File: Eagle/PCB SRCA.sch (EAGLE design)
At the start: 75 parts, among them IC1 DSPIC30F4011-30I_P, IC2 LM324LVIDR, IC3 LMT86QDCKRQ1, IC4 FT232RL-REEL, J1 TBL002A-350-03GR-2OR, J2 TBL002A-350-03GR-2OR, J3 TBL002A-350-03GR-2OR, J4 44914-0801, J5 TBL002A-350-03GR-2OR, J6 44914-0401, Q1 TIP41C, T1 2N3904, T12 2N3904, T13 2N3904, T2 2N3904, T3 2N3904, T4 2N3904, T5 2N3904, T6 2N3904, T7 2N3904

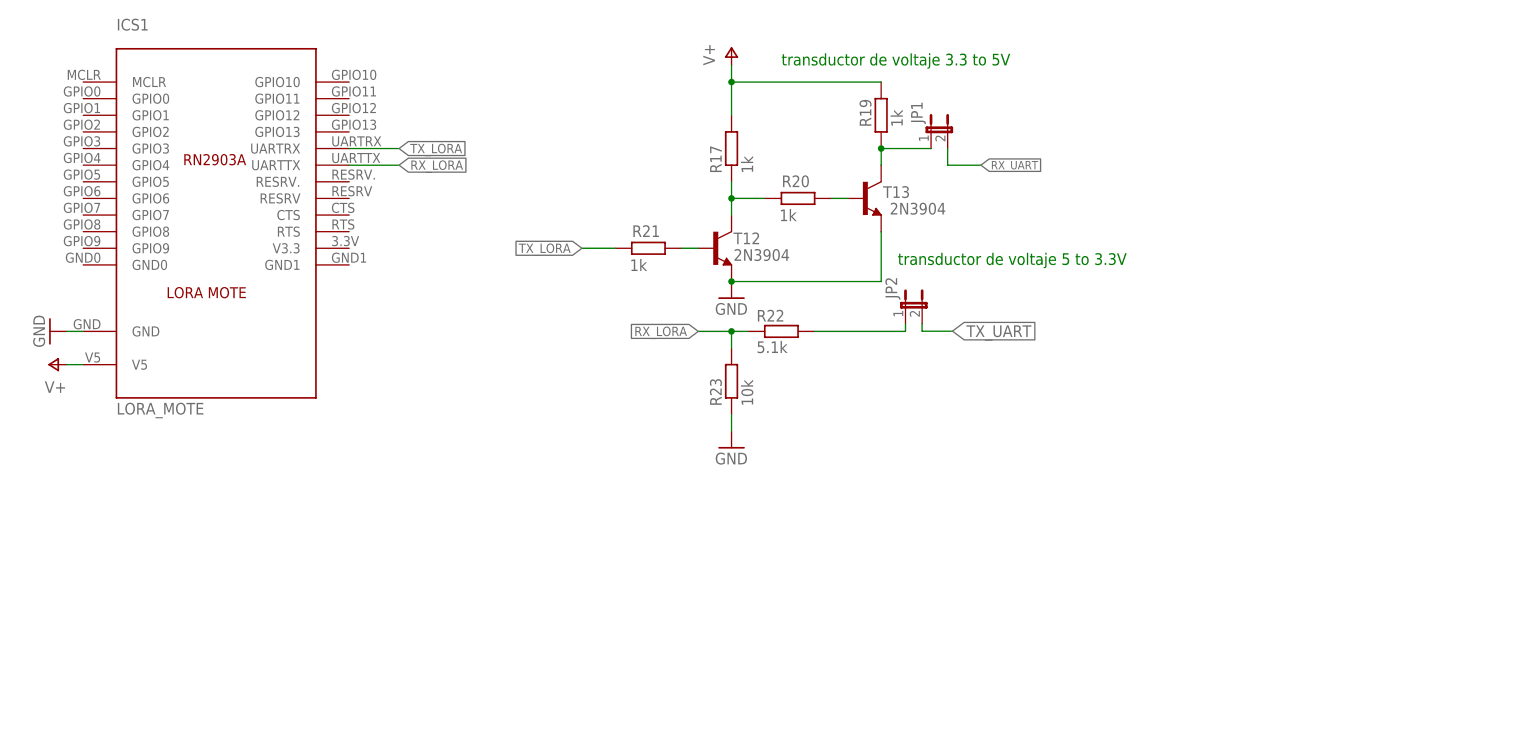
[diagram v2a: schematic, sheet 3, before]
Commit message: 31-08-2021
se agregaron las librerías del proyecto se hizo algunas correciones en la parte de el sensor de temperatura y se hizo se coloco un regulador de 5V a 3.3V para la lora mote
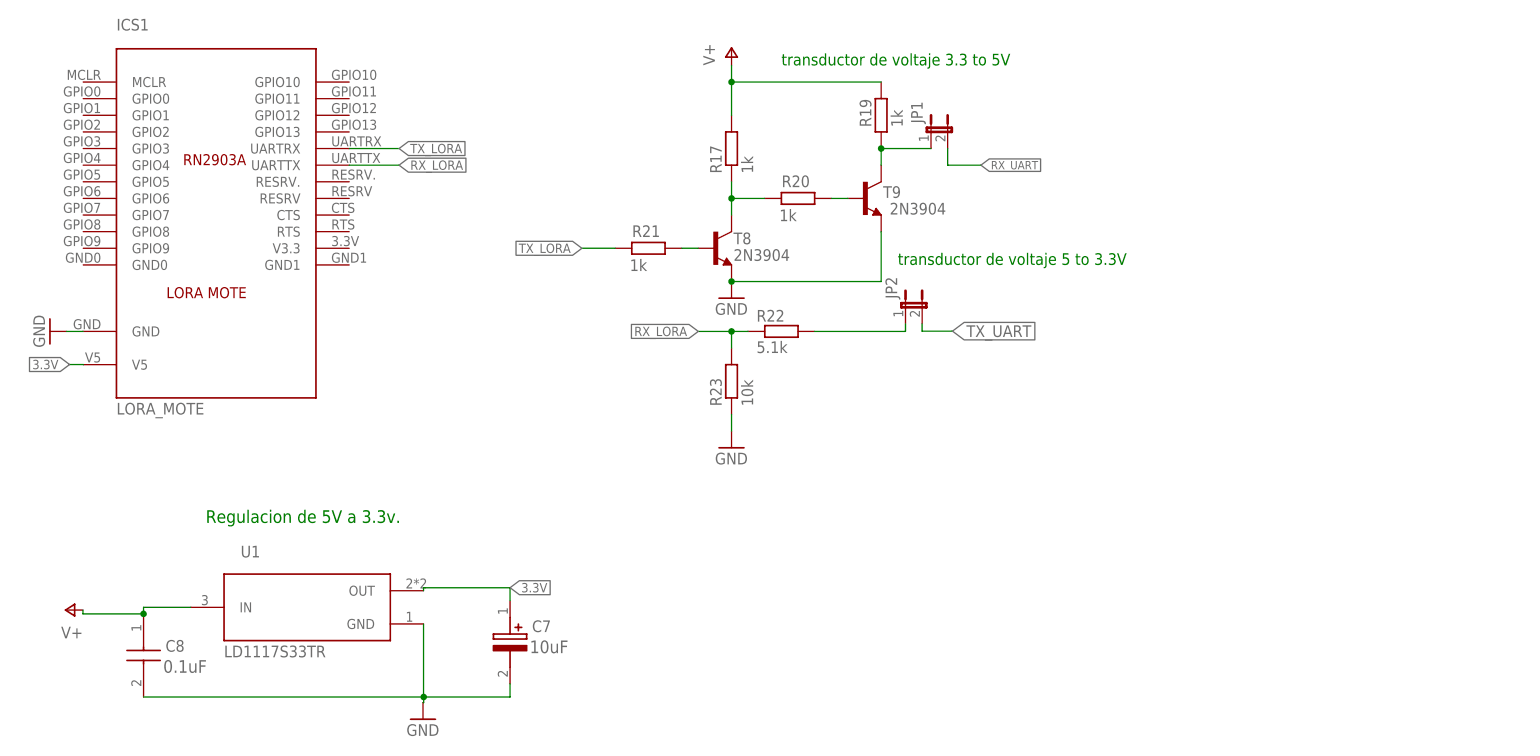
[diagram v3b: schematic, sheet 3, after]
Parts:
- added C7: UUP1C100MCL1GS, UUP1C100MCL1GS:UUP1C100MCL1GS
- added C8: C0805X104K1RAC3316, C0805X104K1RAC3316:C0805X104K1RAC3316
- added R27: RC0805FR-071KL, RC0805FR-071KL:RC0805FR-071KL
- added U1: LD1117S33TR, LD1117S33TR:LD1117S33TR
- renumbered T12 to T8, T13 to T9
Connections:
- new net 3.3V: C7.+, ICS1.V5, U1.OUT
- new net N$14: IC3.OUT, R27.2
- net GND: now also C7.-, C8.2, U1.GND
- net N$27: now also R27.1; no longer IC3.OUT
- net V+: now also C8.1, U1.IN; no longer ICS1.V5
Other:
- note added: "0.1uF"
- note added: "1.5k"
- note added: "Regulacion de 5V a 3.3v."
- moved on the sheet: C1, C5

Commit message: 04-09-2021
cambios de la nueva pcb se agrego cambios del uart entre dspic y lora
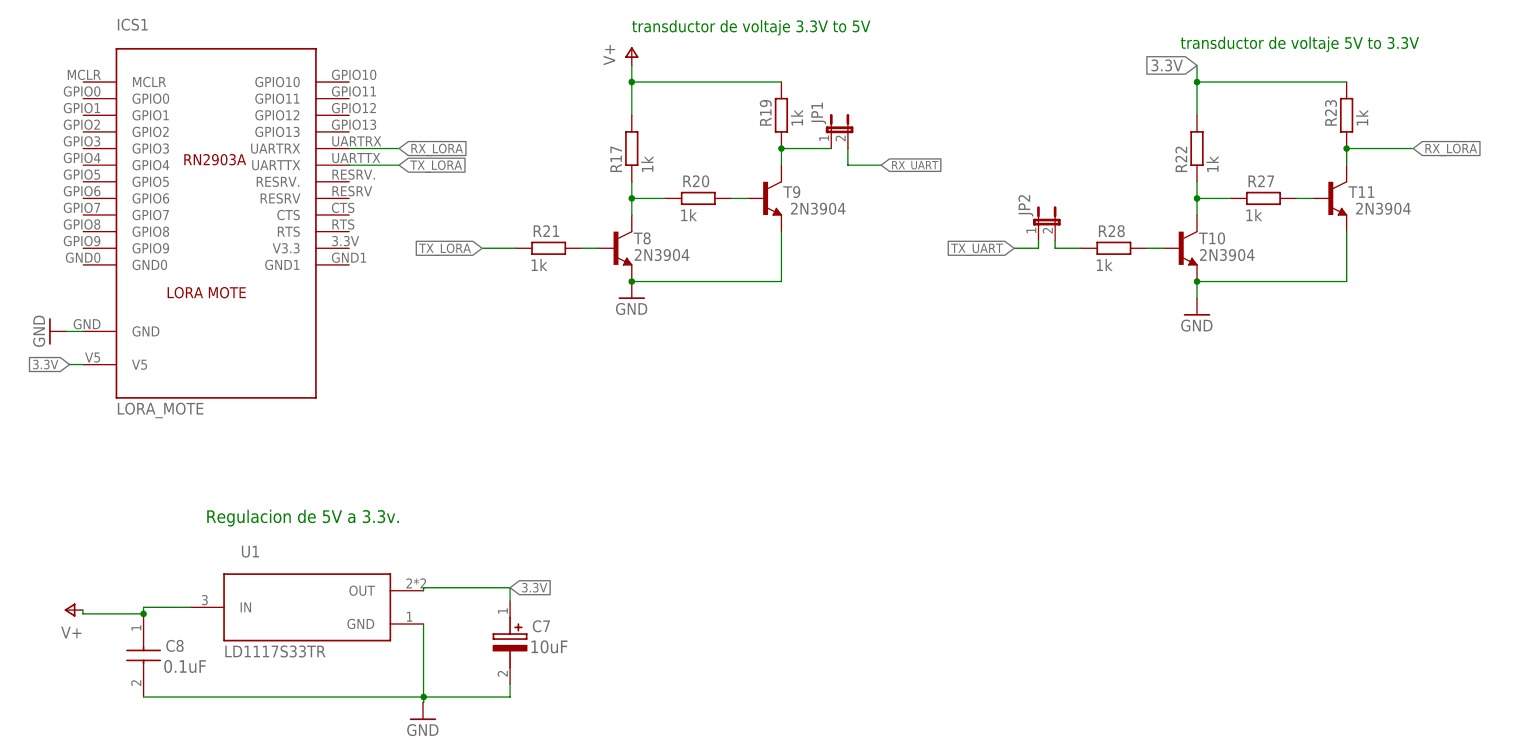
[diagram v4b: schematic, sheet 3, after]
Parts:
- removed C1: (no value), rcl:C-EUC0805
- added R28: 1k, rcl:R-EU_0207/10
- added T10, T11: 2N3904, transistor-neu-to92:2N3904
- IC3: value LMT86QDCKRQ1 -> LM35DZ_NOPB; device LMT86QDCKRQ1:LMT86QDCKRQ1 -> LM35DZ_NOPB:LM35DZ_NOPB
- R15: value 6.8k -> 3.3k
- R16: value 2.7k -> 10k
- R22: value 5.1k -> 1k
- R23: value 10k -> 1k
- R27: value RC0805FR-071KL -> 1k; device RC0805FR-071KL:RC0805FR-071KL -> rcl:R-EU_0207/10
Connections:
- new net N$33: R28.1, T10.B
- new net N$34: R27.1, T11.B
- net 3.3V: now also R22.2, R23.2
- net GND: now also IC3.GND, T10.E, T11.E; no longer C1.2, IC3.GND_1, IC3.GND_2, R23.1
- net N$14: now also IC2.IN3+, IC3.VOUT; no longer IC3.OUT, R27.2
- net N$27: now also R22.1, R27.2, T10.C; no longer C1.1, IC2.IN3+, R27.1
- net N$29: now also JP2.2, R28.2; no longer JP2.1, R22.2
- net RX_LORA: now also ICS1.UARTRX, R23.1, T11.C; no longer ICS1.UARTTX, R22.1, R23.2
- net TX_LORA: now also ICS1.UARTTX; no longer ICS1.UARTRX
- net TX_UART: now also JP2.1; no longer JP2.2
- net V+: now also IC3.+VS; no longer IC3.VDD_1, IC3.VDD_2
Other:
- note added: "transductor de voltaje 3.3V to 5V"
- note added: "transductor de voltaje 5V to 3.3V"
- note removed: "1.5k"
- note removed: "transductor de voltaje 3.3 to 5V"
- note removed: "transductor de voltaje 5 to 3.3V"
- moved on the sheet: JP1, JP2, R17, R19, R20, R21, R22, R23, T8, T9

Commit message: 06-09-2021
se revirtio el cambio de el divisor de voltaje del lora al DSPIC
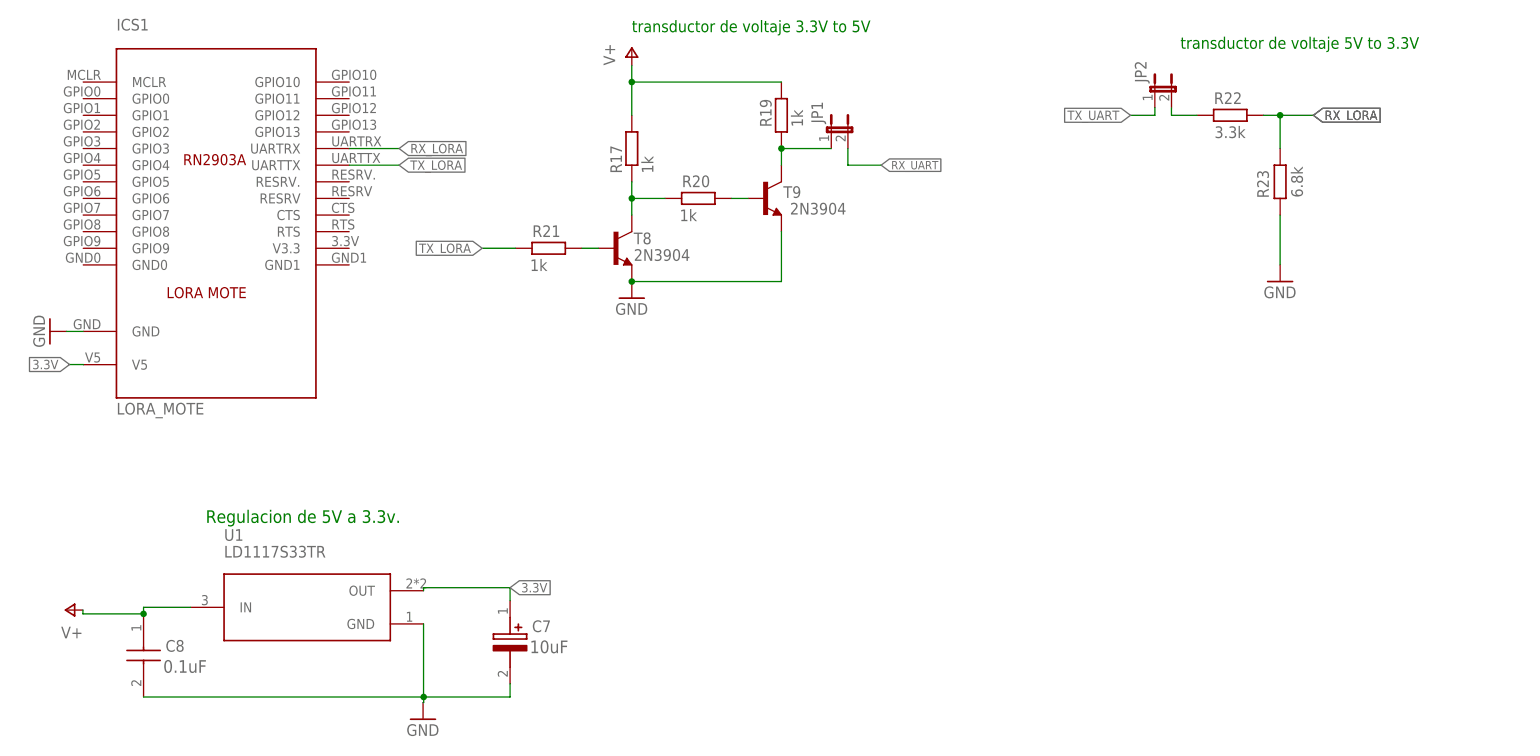
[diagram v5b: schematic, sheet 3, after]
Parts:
- removed R27, R28: 1k, rcl:R-EU_0207/10
- removed T10, T11: 2N3904, transistor-neu-to92:2N3904
- R22: value 1k -> 3.3k
- R23: value 1k -> 6.8k
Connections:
- removed net N$29: JP2.2, R28.2
- removed net N$33: R28.1, T10.B
- removed net N$34: R27.1, T11.B
- net 3.3V: no longer R22.2, R23.2
- net GND: now also R23.2; no longer T10.E, T11.E
- net N$27: now also JP2.2, R22.2; no longer R22.1, R27.2, T10.C
- net RX_LORA: now also R22.1; no longer T11.C
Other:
- note added: "390"
- note added: "Buzzer y Fan"
- note removed: "270"
- moved on the sheet: JP2, R22, R23

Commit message: 06/09/2021
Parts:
- removed C8: C0805X104K1RAC3316, C0805X104K1RAC3316:C0805X104K1RAC3316
- added C1: TAJR104K020RNJ, TAJR104K020RNJ:TAJR104K020RNJ
- C3: value TAJR104K020RNJ -> C0805X104K1RAC3316; device TAJR104K020RNJ:TAJR104K020RNJ -> C0805X104K1RAC3316:C0805X104K1RAC3316
- C5: value C0805X104K1RAC3316 -> UUP1C100MCL1GS; device C0805X104K1RAC3316:C0805X104K1RAC3316 -> UUP1C100MCL1GS:UUP1C100MCL1GS
- C6: value UUP1C100MCL1GS -> C0805X104K1RAC3316; device UUP1C100MCL1GS:UUP1C100MCL1GS -> C0805X104K1RAC3316:C0805X104K1RAC3316
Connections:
- net GND: now also C1.-, C3.1, C5.-, C6.2; no longer C3.-, C5.1, C6.-, C8.2
- net V+: now also C1.+, C3.2, C5.+, C6.1; no longer C3.+, C5.2, C6.+, C8.1
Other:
- moved on the sheet: C2
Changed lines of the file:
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@@
 <part name="R3" library="RC0805FR-071KL" library_urn="urn:adsk.eagle:library:30514931" deviceset="RC0805FR-071KL" device="" package3d_urn="urn:adsk.eagle:package:30514934/2"/>
 <part name="IC2" library="LM324LVIDR" library_urn="urn:adsk.eagle:library:30514898" deviceset="LM324LVIDR" device="" package3d_urn="urn:adsk.eagle:package:30514901/2"/>
+<part name="C1" library="TAJR104K020RNJ" library_urn="urn:adsk.eagle:library:30514861" deviceset="TAJR104K020RNJ" device="" package3d_urn="urn:adsk.eagle:package:30514864/2"/>
 <part name="C2" library="TAJR104K020RNJ" library_urn="urn:adsk.eagle:library:30514861" deviceset="TAJR104K020RNJ" device="" package3d_urn="urn:adsk.eagle:package:30514864/2"/>
-<part name="C3" library="TAJR104K020RNJ" library_urn="urn:adsk.eagle:library:30514861" deviceset="TAJR104K020RNJ" device="" package3d_urn="urn:adsk.eagle:package:30514864/2"/>
 <part name="R15" library="rcl" library_urn="urn:adsk.eagle:library:334" deviceset="R-EU_" device="0207/10" package3d_urn="urn:adsk.eagle:package:23491/2" value="3.3k"/>
 <part name="R16" library="rcl" library_urn="urn:adsk.eagle:library:334" deviceset="R-EU_" device="0207/10" package3d_urn="urn:adsk.eagle:package:23491/2" value="10k"/>
@@
 <part name="R25" library="rcl" library_urn="urn:adsk.eagle:library:334" deviceset="R-EU_" device="0207/10" package3d_urn="urn:adsk.eagle:package:23491/2" value="4.7k"/>
 <part name="R26" library="rcl" library_urn="urn:adsk.eagle:library:334" deviceset="R-EU_" device="0207/10" package3d_urn="urn:adsk.eagle:package:23491/2" value="4.7k"/>
-<part name="C5" library="C0805X104K1RAC3316" library_urn="urn:adsk.eagle:library:30534331" deviceset="C0805X104K1RAC3316" device="" package3d_urn="urn:adsk.eagle:package:30534334/2"/>
+<part name="C3" library="C0805X104K1RAC3316" library_urn="urn:adsk.eagle:library:30534331" deviceset="C0805X104K1RAC3316" device="" package3d_urn="urn:adsk.eagle:package:30534334/2"/>
 <part name="C4" library="C0805X104K1RAC3316" library_urn="urn:adsk.eagle:library:30534331" deviceset="C0805X104K1RAC3316" device="" package3d_urn="urn:adsk.eagle:package:30534334/2"/>
 <part name="IC4" library="FT232RL-REEL" library_urn="urn:adsk.eagle:library:30514882" deviceset="FT232RL-REEL" device="" package3d_urn="urn:adsk.eagle:package:30514885/2"/>
-<part name="C6" library="UUP1C100MCL1GS" library_urn="urn:adsk.eagle:library:30514850" deviceset="UUP1C100MCL1GS" device="" package3d_urn="urn:adsk.eagle:package:30514853/2"/>
+<part name="C5" library="UUP1C100MCL1GS" library_urn="urn:adsk.eagle:library:30514850" deviceset="UUP1C100MCL1GS" device="" package3d_urn="urn:adsk.eagle:package:30514853/2"/>
 <part name="LED7" library="599-0181-007F" library_urn="urn:adsk.eagle:library:30514893" deviceset="599-0181-007F" device="" package3d_urn="urn:adsk.eagle:package:30514896/2"/>
 <part name="LED8" library="599-0181-007F" library_urn="urn:adsk.eagle:library:30514893" deviceset="599-0181-007F" device="" package3d_urn="urn:adsk.eagle:package:30514896/2"/>
@@
 <part name="U1" library="LD1117S33TR" library_urn="urn:adsk.eagle:library:30606054" deviceset="LD1117S33TR" device="" package3d_urn="urn:adsk.eagle:package:30606057/2"/>
 <part name="C7" library="UUP1C100MCL1GS" library_urn="urn:adsk.eagle:library:30514850" deviceset="UUP1C100MCL1GS" device="" package3d_urn="urn:adsk.eagle:package:30514853/2"/>
-<part name="C8" library="C0805X104K1RAC3316" library_urn="urn:adsk.eagle:library:30534331" deviceset="C0805X104K1RAC3316" device="" package3d_urn="urn:adsk.eagle:package:30534334/2"/>
+<part name="C6" library="C0805X104K1RAC3316" library_urn="urn:adsk.eagle:library:30534331" deviceset="C0805X104K1RAC3316" device="" package3d_urn="urn:adsk.eagle:package:30534334/2"/>
 <part name="GND26" library="supply1" library_urn="urn:adsk.eagle:library:371" deviceset="GND" device=""/>
 <part name="GND10" library="supply1" library_urn="urn:adsk.eagle:library:371" deviceset="GND" device=""/>
@@
 <attribute name="VALUE" x="125.85" y="66.72" size="1.778" layer="96" rot="MR0" align="center-left"/>
 </instance>
-<instance part="C2" gate="G$1" x="151.8" y="144.6" smashed="yes" rot="R270">
+<instance part="C1" gate="G$1" x="151.8" y="144.6" smashed="yes" rot="R270">
 <attribute name="NAME" x="153.45" y="142.41" size="1.778" layer="95" align="center-left"/>
 </instance>
-<instance part="C3" gate="G$1" x="162.8" y="145" smashed="yes" rot="R270">
+<instance part="C2" gate="G$1" x="162.8" y="145" smashed="yes" rot="R270">
 <attribute name="NAME" x="164.65" y="142.71" size="1.778" layer="95" align="center-left"/>
 </instance>
@@
 </segment>
 <segment>
-<pinref part="C2" gate="G$1" pin="-"/>
+<pinref part="C1" gate="G$1" pin="-"/>
 <pinref part="GND5" gate="1" pin="GND"/>
 <wire x1="151.8" y1="131.9" x2="151.8" y2="127" width="0.1524" layer="91"/>
 <wire x1="151.8" y1="127" x2="157.48" y2="127" width="0.1524" layer="91"/>
-<pinref part="C3" gate="G$1" pin="-"/>
+<pinref part="C2" gate="G$1" pin="-"/>
 <wire x1="157.48" y1="127" x2="162.8" y2="127" width="0.1524" layer="91"/>
 <wire x1="162.8" y1="127" x2="162.8" y2="132.3" width="0.1524" layer="91"/>
@@
 </segment>
 <segment>
-<pinref part="C2" gate="G$1" pin="+"/>
+<pinref part="C1" gate="G$1" pin="+"/>
 <wire x1="151.8" y1="144.6" x2="151.8" y2="149.3" width="0.1524" layer="91"/>
 <pinref part="P+13" gate="1" pin="V+"/>
 <wire x1="151.8" y1="149.3" x2="157.48" y2="149.3" width="0.1524" layer="91"/>
 <wire x1="157.48" y1="149.3" x2="157.48" y2="154.94" width="0.1524" layer="91"/>
-<pinref part="C3" gate="G$1" pin="+"/>
+<pinref part="C2" gate="G$1" pin="+"/>
 <wire x1="162.8" y1="145" x2="162.8" y2="149.4" width="0.1524" layer="91"/>
 <wire x1="162.8" y1="149.4" x2="157.4" y2="149.4" width="0.1524" layer="91"/>
@@
 <attribute name="NAME" x="233.68" y="57.15" size="1.778" layer="95" rot="R90" align="center-left"/>
 </instance>
-<instance part="C5" gate="G$1" x="14" y="9.1" smashed="yes" rot="R90">
+<instance part="C3" gate="G$1" x="14" y="9.1" smashed="yes" rot="R90">
 <attribute name="NAME" x="16.65" y="10.99" size="1.778" layer="95" rot="R90" align="center-left"/>
 </instance>
@@
 <attribute name="VALUE" x="45.01" y="60.68" size="1.778" layer="96" align="center-left"/>
 </instance>
-<instance part="C6" gate="G$1" x="25.7" y="20.6" smashed="yes" rot="R270">
+<instance part="C5" gate="G$1" x="25.7" y="20.6" smashed="yes" rot="R270">
 <attribute name="NAME" x="21.55" y="15.91" size="1.778" layer="95" rot="R270" align="center-left"/>
 </instance>
@@
 <wire x1="39" y1="5.54" x2="39" y2="6" width="0.1524" layer="91"/>
 <junction x="39" y="6"/>
-<pinref part="C5" gate="G$1" pin="1"/>
+<pinref part="C3" gate="G$1" pin="1"/>
 <wire x1="14" y1="9.1" x2="14" y2="6" width="0.1524" layer="91"/>
 <wire x1="14" y1="6" x2="25.7" y2="6" width="0.1524" layer="91"/>
@@
 <wire x1="25.7" y1="6" x2="39" y2="6" width="0.1524" layer="91"/>
 <wire x1="76" y1="8" x2="76" y2="6" width="0.1524" layer="91"/>
-<pinref part="C6" gate="G$1" pin="-"/>
+<pinref part="C5" gate="G$1" pin="-"/>
 <wire x1="25.7" y1="7.9" x2="25.7" y2="6" width="0.1524" layer="91"/>
 </segment>
@@
 <segment>
 <pinref part="P+21" gate="1" pin="V+"/>
-<pinref part="C5" gate="G$1" pin="2"/>
+<pinref part="C3" gate="G$1" pin="2"/>
 <wire x1="20" y1="26.46" x2="14" y2="26.46" width="0.1524" layer="91"/>
 <wire x1="14" y1="26.46" x2="14" y2="21.8" width="0.1524" layer="91"/>
-<pinref part="C6" gate="G$1" pin="+"/>
+<pinref part="C5" gate="G$1" pin="+"/>
 <wire x1="20" y1="26.46" x2="25.7" y2="26.46" width="0.1524" layer="91"/>
 <wire x1="25.7" y1="26.46" x2="25.7" y2="20.6" width="0.1524" layer="91"/>
@@
 <sheet>
 <plain>
-<text x="101.6" y="182.88" size="1.778" layer="91">transductor de voltaje 3.3V to 5V</text>
-<text x="185.42" y="180.34" size="1.778" layer="91">transductor de voltaje 5V to 3.3V</text>
+<text x="109.22" y="177.8" size="1.778" layer="91">transductor de voltaje 3.3V to 5V</text>
+<text x="187.96" y="177.8" size="1.778" layer="91">transductor de voltaje 5V to 3.3V</text>
 <text x="36.5" y="107.9" size="1.9304" layer="91">Regulacion de 5V a 3.3v.</text>
 <text x="30" y="85" size="1.9304" layer="95">0.1uF</text>
@@
 <attribute name="NAME" x="86.35" y="92.11" size="1.778" layer="95" align="center-left"/>
 </instance>
-<instance part="C8" gate="G$1" x="27" y="94" smashed="yes" rot="R270">
+<instance part="C6" gate="G$1" x="27" y="94" smashed="yes" rot="R270">
 <attribute name="NAME" x="30.35" y="89.11" size="1.778" layer="95" align="center-left"/>
 </instance>
@@
 </segment>
 <segment>
-<pinref part="C8" gate="G$1" pin="2"/>
+<pinref part="C6" gate="G$1" pin="2"/>
 <pinref part="C7" gate="G$1" pin="-"/>
 <wire x1="27" y1="81.3" x2="69.78" y2="81.3" width="0.1524" layer="91"/>
@@
 <segment>
 <pinref part="U1" gate="G$1" pin="IN"/>
-<pinref part="C8" gate="G$1" pin="1"/>
+<pinref part="C6" gate="G$1" pin="1"/>
 <wire x1="34.22" y1="95" x2="27" y2="95" width="0.1524" layer="91"/>
 <wire x1="27" y1="95" x2="27" y2="94" width="0.1524" layer="91"/>

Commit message: 23-09-2021
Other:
- note added: "PGC"
- note added: "PGD"
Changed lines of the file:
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@@
 <text x="221" y="73" size="1.778" layer="95" rot="R90">1k</text>
 <text x="203.2" y="177.8" size="2.54" layer="91">Buzzer y Fan</text>
+<text x="175.26" y="167.64" size="1.778" layer="91">PGD</text>
+<text x="175.26" y="165.1" size="1.778" layer="91">PGC</text>
 </plain>
 <instances>
